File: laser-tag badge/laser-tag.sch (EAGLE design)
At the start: 36 parts, among them Q1 2N7002ET1G, U1 MKL27Z256VLH4

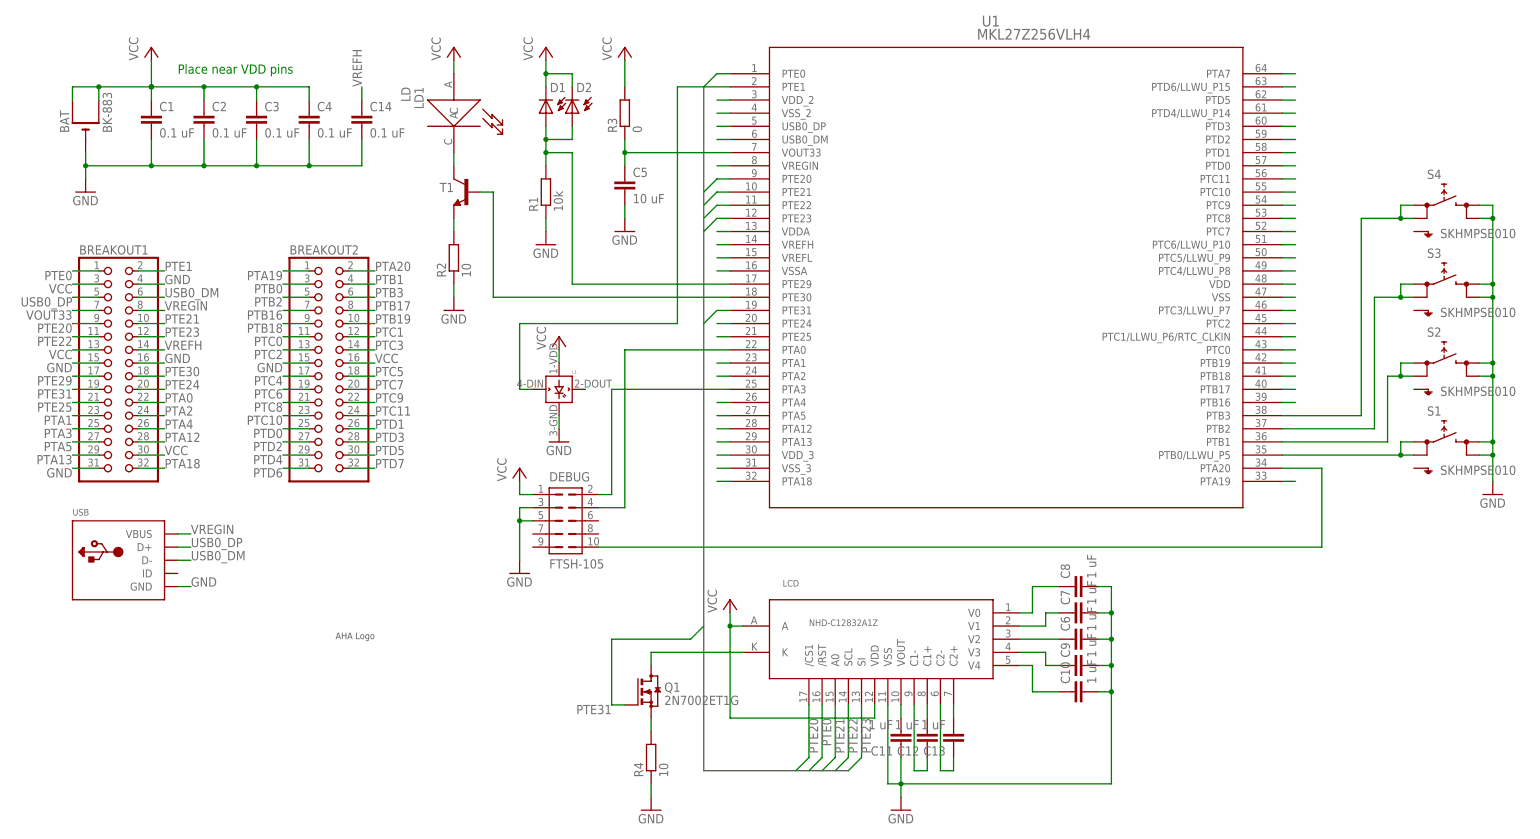
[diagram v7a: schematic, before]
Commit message: Added a voltage divider for VREFH input
This way we can get higher resolution in the range of voltages
we get from the photodiodes.
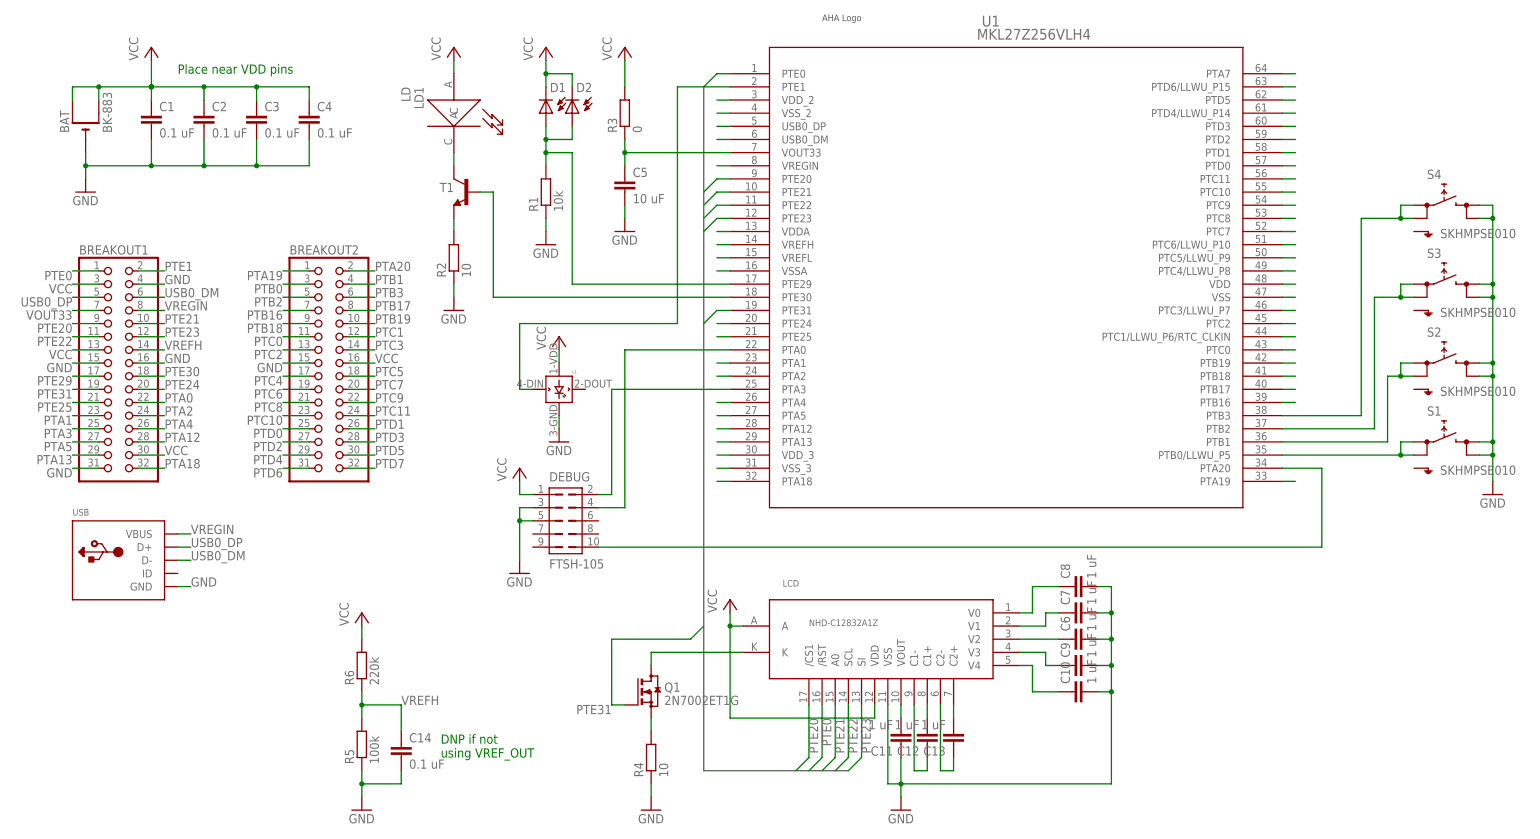
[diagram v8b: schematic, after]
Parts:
- added R5: 100k, rcl:R-EU_R0603
- added R6: 220k, rcl:R-EU_R0603
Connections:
- net GND: now also R5.1
- net VCC: now also R6.2
- net VREFH: now also R5.2, R6.1
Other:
- note added: "DNP if not using VREF_OUT"
- moved on the sheet: C14
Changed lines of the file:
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@@
 <part name="C14" library="rcl" deviceset="C-EU" device="C0603K" value="0.1 uF"/>
 <part name="Q1" library="transistor-small-signal" deviceset="BSS123" device="" value="2N7002ET1G"/>
+<part name="GND10" library="supply1" deviceset="GND" device=""/>
+<part name="R5" library="rcl" deviceset="R-EU_" device="R0603" value="100k"/>
+<part name="R6" library="rcl" deviceset="R-EU_" device="R0603" value="220k"/>
+<part name="P+8" library="supply1" deviceset="VCC" device=""/>
 </parts>
 <sheets>
@@
 <plain>
 <text x="-96.52" y="99.06" size="1.778" layer="91">Place near VDD pins</text>
+<text x="-45.72" y="-33.02" size="1.778" layer="91">DNP if not
+using VREF_OUT</text>
 </plain>
 <instances>
@@
 <attribute name="NAME" x="-19.558" y="95.504" size="1.778" layer="95"/>
 </instance>
-<instance part="U$1" gate="G$1" x="-66.04" y="-10.16"/>
+<instance part="U$1" gate="G$1" x="27.94" y="109.22"/>
 <instance part="L1" gate="G$1" x="-22.86" y="38.1"/>
 <instance part="P+6" gate="VCC" x="-22.86" y="48.26"/>
 <instance part="GND9" gate="1" x="-22.86" y="27.94"/>
-<instance part="C14" gate="G$1" x="-60.96" y="91.44"/>
+<instance part="C14" gate="G$1" x="-53.34" y="-30.48"/>
 <instance part="Q1" gate="G$1" x="-5.08" y="-20.32"/>
+<instance part="GND10" gate="1" x="-60.96" y="-43.18"/>
+<instance part="R5" gate="G$1" x="-60.96" y="-30.48" rot="R90"/>
+<instance part="R6" gate="G$1" x="-60.96" y="-15.24" rot="R90"/>
+<instance part="P+8" gate="VCC" x="-60.96" y="-5.08"/>
 </instances>
 <busses>
@@
 <nets>
 <net name="GND" class="0">
+<segment>
+<pinref part="C14" gate="G$1" pin="2"/>
+<wire x1="-60.96" y1="-40.64" x2="-60.96" y2="-38.1" width="0.1524" layer="91"/>
+<wire x1="-60.96" y1="-38.1" x2="-53.34" y2="-38.1" width="0.1524" layer="91"/>
+<wire x1="-53.34" y1="-38.1" x2="-53.34" y2="-35.56" width="0.1524" layer="91"/>
+<pinref part="GND10" gate="1" pin="GND"/>
+<pinref part="R5" gate="G$1" pin="1"/>
+<wire x1="-60.96" y1="-38.1" x2="-60.96" y2="-35.56" width="0.1524" layer="91"/>
+<junction x="-60.96" y="-38.1"/>
+</segment>
 <segment>
 <pinref part="BAT" gate="G$1" pin="-"/>
@@
 <wire x1="-71.12" y1="81.28" x2="-71.12" y2="86.36" width="0.1524" layer="91"/>
 <junction x="-81.28" y="81.28"/>
-<pinref part="C14" gate="G$1" pin="2"/>
-<wire x1="-71.12" y1="81.28" x2="-60.96" y2="81.28" width="0.1524" layer="91"/>
-<wire x1="-60.96" y1="81.28" x2="-60.96" y2="86.36" width="0.1524" layer="91"/>
-<junction x="-71.12" y="81.28"/>
 </segment>
 <segment>
@@
 <wire x1="-22.86" y1="45.72" x2="-22.86" y2="43.18" width="0.1524" layer="91"/>
 </segment>
+<segment>
+<pinref part="R6" gate="G$1" pin="2"/>
+<pinref part="P+8" gate="VCC" pin="VCC"/>
+<wire x1="-60.96" y1="-10.16" x2="-60.96" y2="-7.62" width="0.1524" layer="91"/>
+</segment>
 </net>
 <net name="PTA3" class="0">
@@
 <segment>
 <pinref part="C14" gate="G$1" pin="1"/>
-<wire x1="-60.96" y1="93.98" x2="-60.96" y2="96.52" width="0.1524" layer="91"/>
-<label x="-60.96" y="96.52" size="1.778" layer="95" rot="R90"/>
+<wire x1="-53.34" y1="-27.94" x2="-53.34" y2="-22.86" width="0.1524" layer="91"/>
+<label x="-53.34" y="-22.86" size="1.778" layer="95"/>
+<pinref part="R5" gate="G$1" pin="2"/>
+<pinref part="R6" gate="G$1" pin="1"/>
+<wire x1="-60.96" y1="-25.4" x2="-60.96" y2="-22.86" width="0.1524" layer="91"/>
+<wire x1="-60.96" y1="-22.86" x2="-60.96" y2="-20.32" width="0.1524" layer="91"/>
+<wire x1="-60.96" y1="-22.86" x2="-53.34" y2="-22.86" width="0.1524" layer="91"/>
+<junction x="-60.96" y="-22.86"/>
 </segment>
 </net>
@@
 </schematic>
 </drawing>
+<compatibility>
+<note version="6.3" minversion="6.2.2" severity="warning">
+Since Version 6.2.2 text objects can contain more than one line,
+which will not be processed correctly with this version.
+</note>
+</compatibility>
 </eagle>
